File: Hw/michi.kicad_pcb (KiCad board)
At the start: 2 copper layers, 93.7 x 120.9 mm, 55 parts, among them J1 Conn_01x02, J2 Conn_Right, P1 USB_C_Plug_USB2.0, P6 D, SW1 SW_Push, U1 RP2040, U2 NCP1117ST33T3G, U3 W25Q128JVS, Y1 Crystal

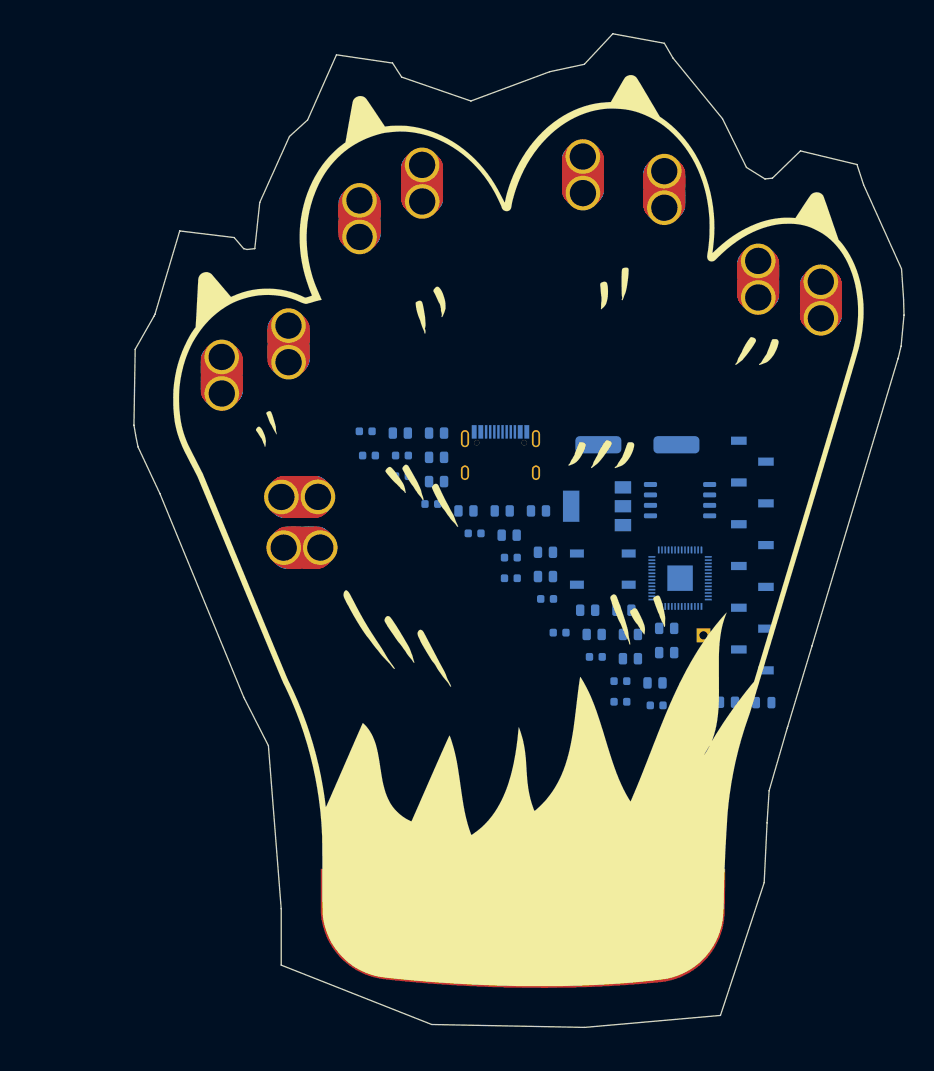
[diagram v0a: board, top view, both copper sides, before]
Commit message: Added Art Michi
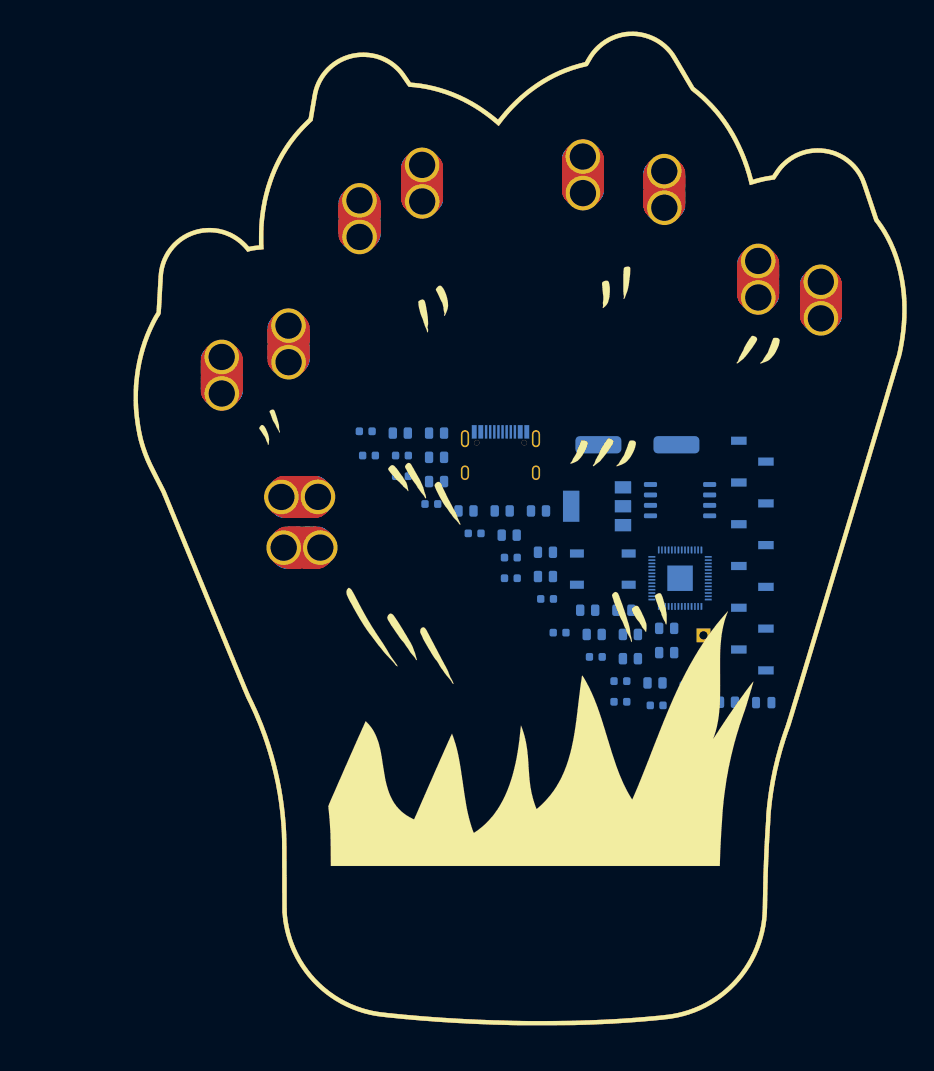
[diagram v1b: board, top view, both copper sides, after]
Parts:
- removed the Ref** at (117.1, 99.1)
- added Ref**: Val**, PCB_Michi_Act, F.Cu at (117.3, 98.8)
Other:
- board outline removed

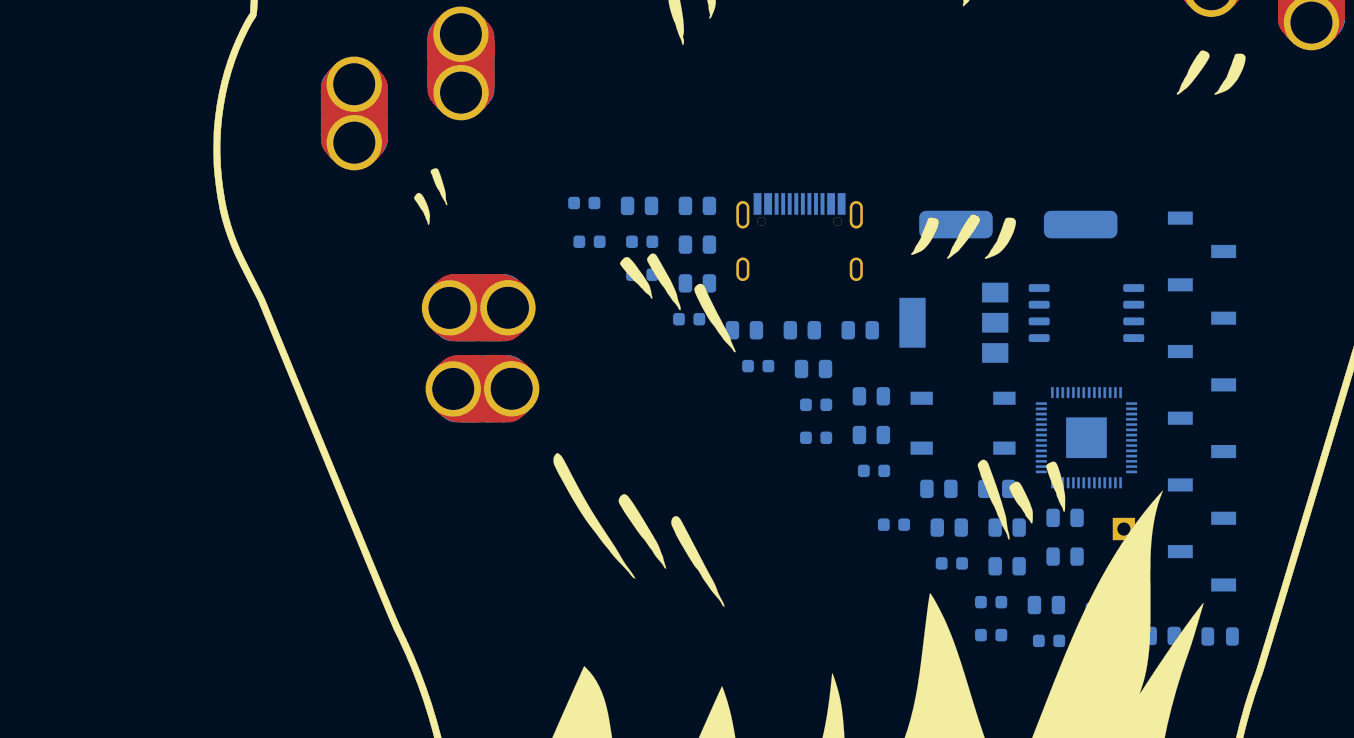
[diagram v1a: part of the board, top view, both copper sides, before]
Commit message: Floorplan placement
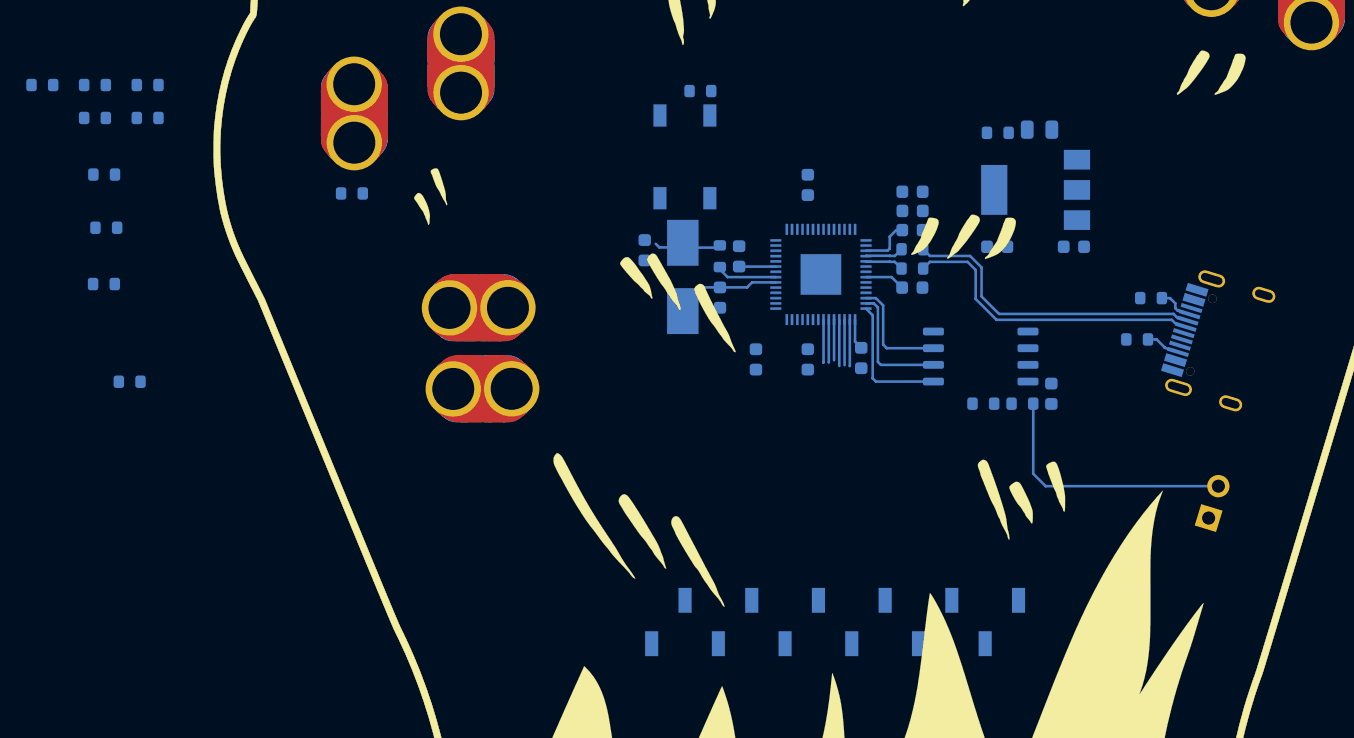
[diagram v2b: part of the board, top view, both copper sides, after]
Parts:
- removed R19, R20: 22M, Resistor_SMD:R_0805_2012Metric
- R1, R10, R11, R12, R14, R15, R16, R17, R18, R2, R21, R3, R4, R5, R6, R7, R8, R9: footprint Resistor_SMD:R_0805_2012Metric -> Resistor_SMD:R_0603_1608Metric
- R13: value DNF -> DNP; footprint Resistor_SMD:R_0805_2012Metric -> Resistor_SMD:R_0603_1608Metric
- Y1: footprint Library:ABLS-12.000MHZ-B4-T -> Crystal:Crystal_SMD_5032-2Pin_5.0x3.2mm_HandSoldering
- moved R16 88.1 mm to (61.3, 78.0)
- moved R18 83.1 mm to (62.0, 84.8)
- moved R12 77.2 mm to (62.2, 88.9)
- moved R15 74.9 mm to (57.3, 78.0)
- moved R17 70.6 mm to (65.3, 80.5)
- moved R10 63.9 mm to (61.3, 80.5)
- moved R9 59.7 mm to (80.9, 86.2)
- moved R6 57.7 mm to (62.0, 93.2)
- moved R7 56.5 mm to (64.0, 100.6)
- moved R14 53.2 mm to (65.3, 78.0)
- moved D1 41.0 mm to (133.2, 81.4)
- moved R5 40.3 mm to (130.1, 81.6)
- moved R21 38.3 mm to (107.4, 78.5), turned to 0 degrees
- moved C3 33.0 mm to (108.9, 94.2), turned to 90 degrees
- moved J2 32.6 mm to (117.7, 118.9), turned to -90 degrees
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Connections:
- net Net-(R3-Pad1) renamed /DR-
- net Net-(R4-Pad1) renamed /DR+
- J2 pad 6: unconnected-(J2-Pad6) -> /IO24
- J2 pad 7: unconnected-(J2-Pad7) -> /IO10
- J2 pad 8: unconnected-(J2-Pad8) -> /IO11
- J2 pad 9: unconnected-(J2-Pad9) -> /IO23
- R8 pad 1: Net-(C4-Pad2) -> /XOUT
- R8 pad 2: /XOUT -> Net-(C4-Pad2)
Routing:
- net /D-: track 0.00 -> 22.8 mm
- net /D+: track 0.00 -> 22.7 mm
- net Net-(J1-Pad2): track 0.00 -> 19.8 mm
- net /SS: track 0.00 -> 10.3 mm
- net +1V1: track 0.00 -> 9.81 mm
- net /SD1: track 0.00 -> 9.50 mm
- net /SD2: track 0.00 -> 8.46 mm
- net /XIN: track 0.00 -> 7.23 mm
- net Net-(C4-Pad2): track 0.00 -> 5.00 mm
- net /XOUT: track 0.00 -> 4.51 mm
- net /IO0: track 0.00 -> 3.54 mm
- net /IO2: track 0.00 -> 3.53 mm
- net /IO1: track 0.00 -> 3.48 mm
- net /IO5: track 0.00 -> 3.29 mm
- net /IO4: track 0.00 -> 3.26 mm
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
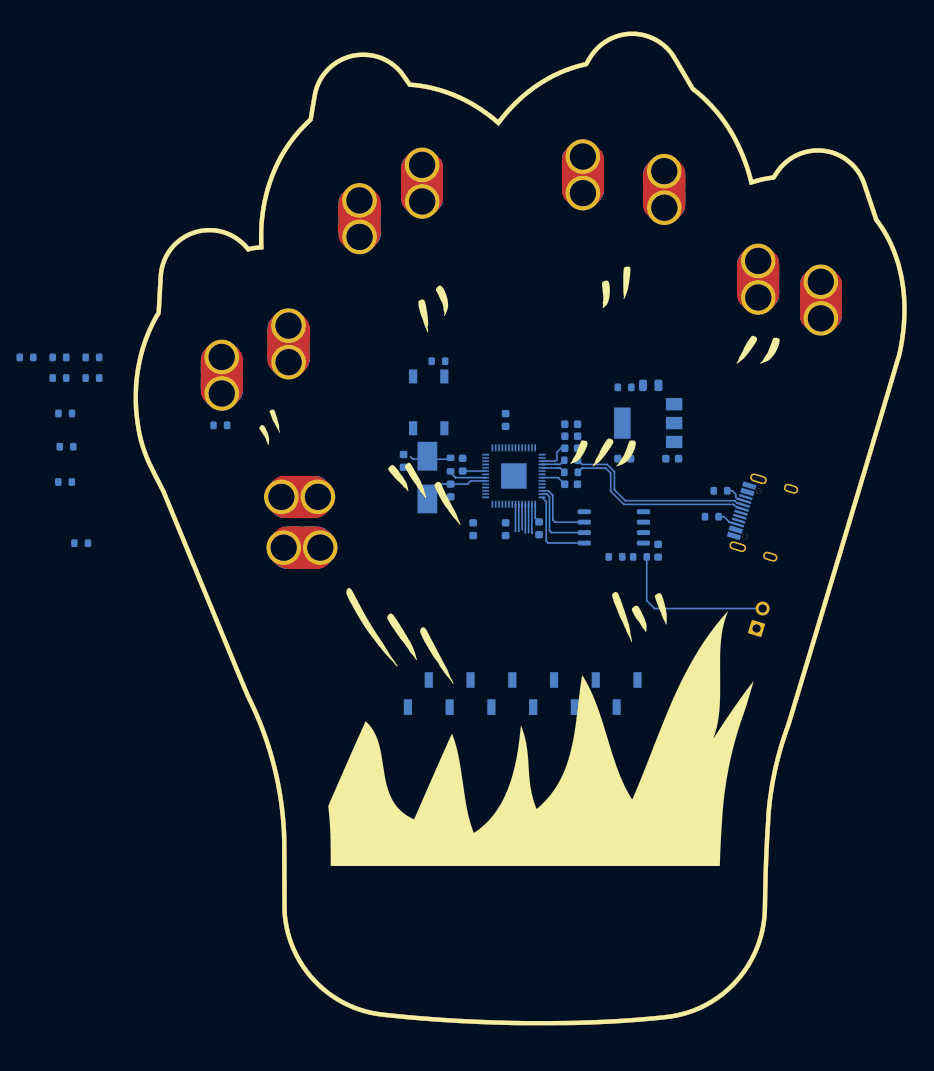
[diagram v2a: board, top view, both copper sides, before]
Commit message: Started PCB routing
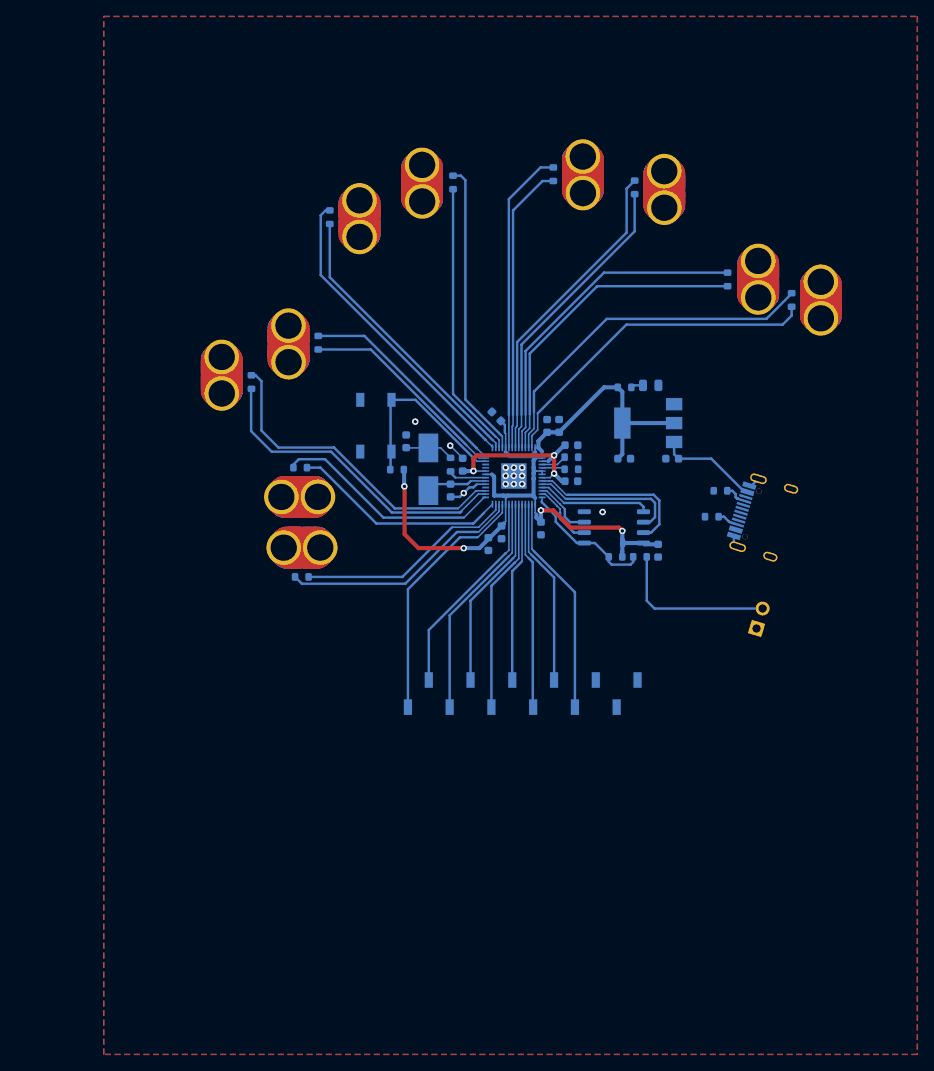
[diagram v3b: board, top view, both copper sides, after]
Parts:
- removed Ref**: Val**, PCB_Michi_Act
- moved R18 89.5 mm to (150.4, 71.0), turned to 90 degrees
- moved R17 78.2 mm to (142.6, 68.5), turned to 90 degrees
- moved R16 73.0 mm to (131.3, 57.3), turned to 90 degrees
- moved R15 67.9 mm to (121.4, 55.7), turned to 90 degrees
- moved R14 48.8 mm to (109.2, 56.7), turned to -90 degrees
- moved R12 42.5 mm to (94.2, 60.9), turned to 90 degrees
- moved R10 31.8 mm to (92.8, 76.2), turned to -90 degrees
- moved R6 31.0 mm to (90.8, 104.7)
- moved R7 28.2 mm to (90.6, 91.4), turned to 0 degrees
- moved R21 14.1 mm to (102.4, 91.6)
- moved SW1 7.03 mm to (99.8, 86.3)
- moved R9 6.48 mm to (84.7, 81.0), turned to -90 degrees
- moved C13 2.94 mm to (120.6, 86.3), turned to 90 degrees
- moved C11 2.59 mm to (113.5, 100.7)
- moved C4 2.40 mm to (103.5, 88.2), turned to -90 degrees
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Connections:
- J2 pad 1: /IO25 -> /IO8
- J2 pad 2: /IO26 -> /IO7
- J2 pad 3: /IO27 -> /IO6
- J2 pad 4: /IO28 -> /IO5
- J2 pad 5: /IO29 -> /IO4
- J2 pad 6: /IO24 -> /IO3
- J2 pad 7: /IO10 -> /IO2
- J2 pad 8: /IO11 -> /IO1
- J2 pad 9: /IO23 -> /IO0
- R10 pad 1: /IO15 -> /IO17
- R10 pad 2: /IO14 -> /IO16
- R12 pad 1: /IO5 -> /IO19
- R12 pad 2: /IO4 -> /IO18
- R14 pad 1: /IO17 -> /IO21
- R14 pad 2: /IO16 -> /IO20
- R15 pad 1: /IO7 -> /IO23
- R15 pad 2: /IO6 -> /IO22
- R16 pad 1: /IO19 -> /IO25
- R16 pad 2: /IO18 -> /IO24
- R17 pad 1: /IO9 -> /IO27
- R17 pad 2: /IO8 -> /IO26
- R18 pad 1: /IO22 -> /IO29
- R18 pad 2: /IO21 -> /IO28
- R6 pad 1: /IO1 -> /IO10
- R6 pad 2: /IO0 -> /IO9
- R7 pad 1: /IO13 -> /IO12
- R7 pad 2: /IO12 -> /IO11
- R9 pad 1: /IO3 -> /IO14
- R9 pad 2: /IO2 -> /IO13
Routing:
- net +3V3: track 2.35 -> 106.5 mm, vias 0 -> 4
- net /IO28: track 0.00 -> 43.4 mm
- net /IO29: track 0.00 -> 41.4 mm
- net /IO26: track 0.00 -> 40.5 mm
- net /IO14: track 0.00 -> 39.6 mm
- net /IO27: track 0.00 -> 39.1 mm
- net /IO13: track 0.00 -> 38.7 mm
- net /IO24: track 0.00 -> 38.5 mm
- net /IO18: track 0.00 -> 38.3 mm
- net /IO22: track 0.00 -> 37.3 mm
- net /IO25: track 0.00 -> 36.7 mm
- net /IO21: track 0.00 -> 36.2 mm
- net /IO19: track 0.00 -> 35.6 mm
- net /IO23: track 0.00 -> 35.3 mm
- net /IO20: track 0.00 -> 33.8 mm
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- added copper zone on B.Cu, net GND
- added copper zone on F.Cu, net GND

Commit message: Fixed PCB outline
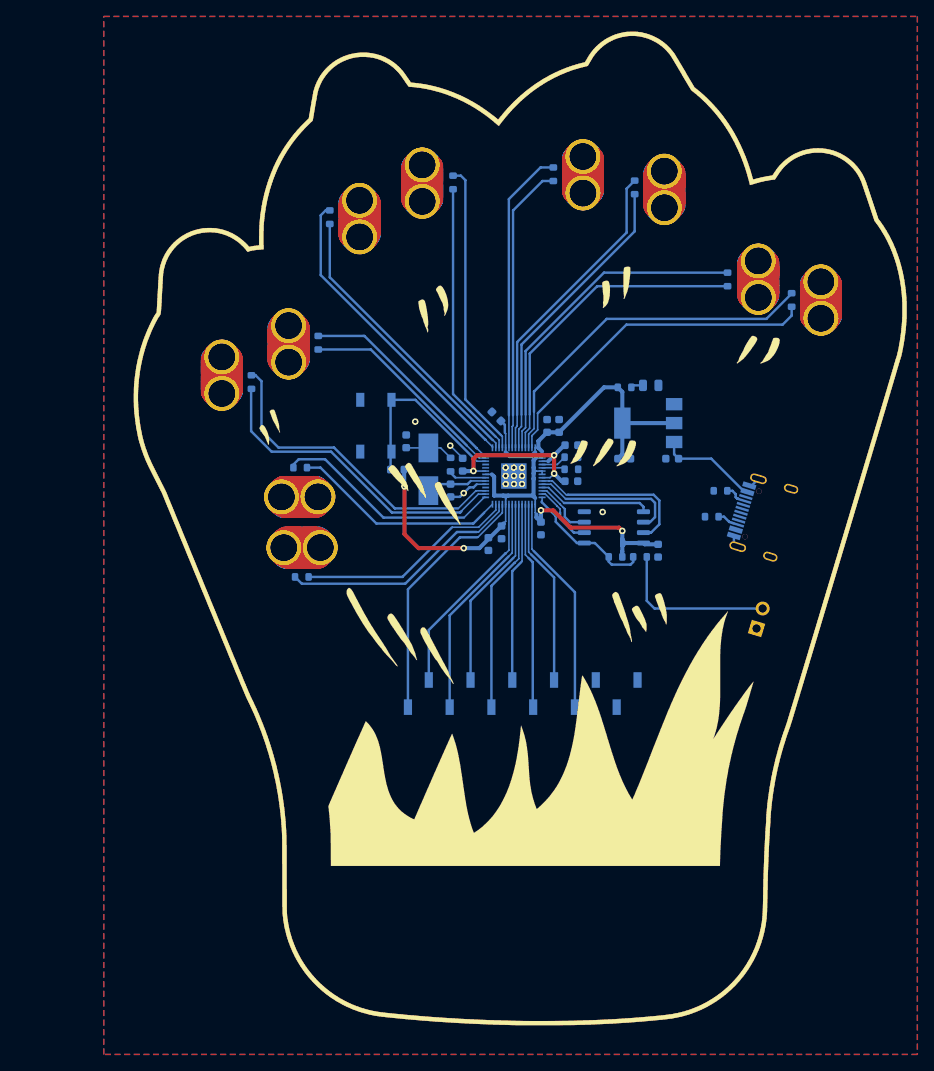
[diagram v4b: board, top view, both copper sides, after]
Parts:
- added P6: D, SEWALLI_renew, F.Cu at (135.0, 57.4)
- added P6: D, SEWALLI_renew, F.Cu at (125.1, 55.6)
- added P6: D, SEWALLI_renew, F.Cu at (146.4, 68.3)
- added P6: D, SEWALLI_renew, F.Cu at (81.1, 80.0)
- added P6: D, SEWALLI_renew, F.Cu at (105.5, 56.6)
- added P6: D, SEWALLI_renew, F.Cu at (90.4, 94.9)
- added P6: D, SEWALLI_renew, F.Cu at (154.0, 70.9)
- added P6: D, SEWALLI_renew, F.Cu at (90.7, 101.1)
- added P6: D, SEWALLI_renew, F.Cu at (89.2, 76.2)
- added P6: D, SEWALLI_renew, F.Cu at (97.9, 61.0)
- added Ref**: Val**, PCB_Michi_Act, F.Cu at (117.4, 98.8)
